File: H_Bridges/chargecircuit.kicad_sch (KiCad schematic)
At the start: 31 parts, among them J2 USB4085-GF-A_REVB, Q10 PMOS, Q9 PMOS, U2 max1898eub42+T, U3 TPS61023DRLR

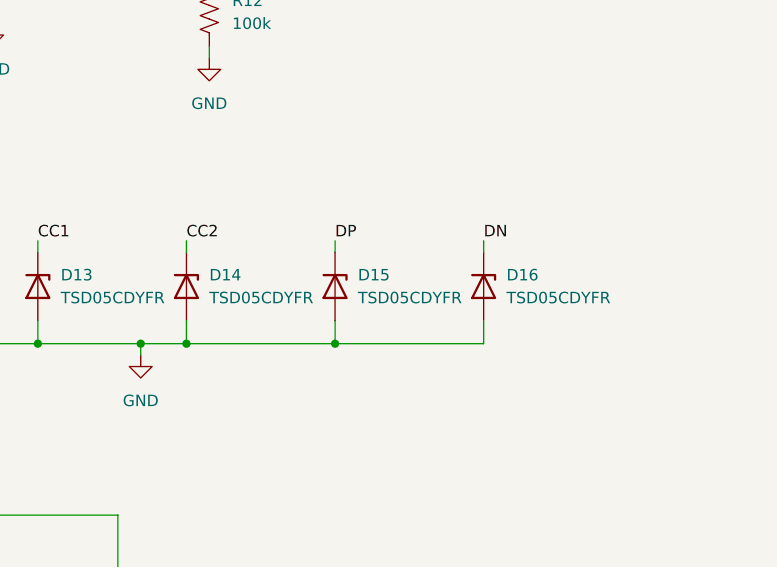
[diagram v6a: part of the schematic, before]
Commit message: placement fixes
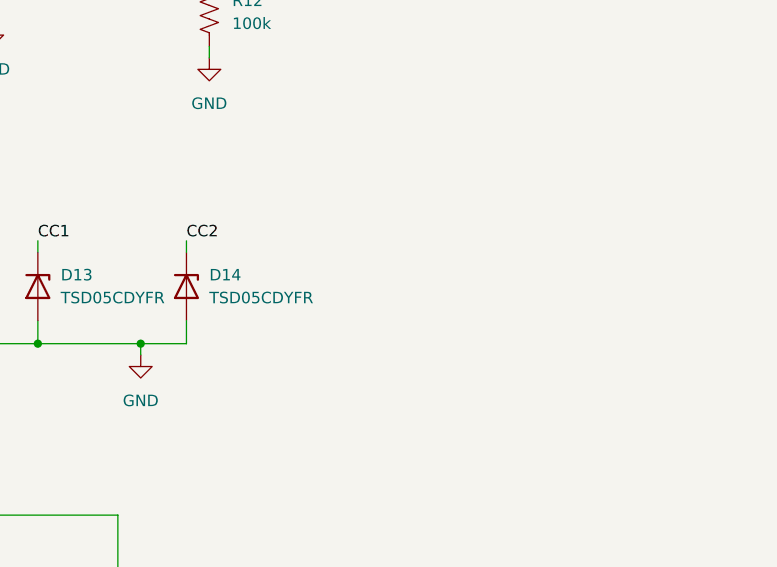
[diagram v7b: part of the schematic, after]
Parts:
- removed D15, D16: TSD05CDYFR, Footprints:TVS_SOD2_DYF_TEX-L, symbol Diode:PTVS5V0Z1USK
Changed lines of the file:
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@@
 	)
 	(junction
-		(at 241.3 91.44)
-		(diameter 0)
-		(color 0 0 0 0)
-	)
-	(junction
 		(at 173.99 138.43)
 		(diameter 0)
@@
 	)
 	(junction
-		(at 224.79 91.44)
-		(diameter 0)
-		(color 0 0 0 0)
-	)
-	(junction
 		(at 106.68 80.01)
 		(diameter 0)
@@
 	(wire
 		(pts
-			(xy 257.81 80.01) (xy 257.81 81.28)
-		)
-		(stroke
-			(width 0)
-			(type default)
-		)
-	)
-	(wire
-		(pts
 			(xy 147.32 110.49) (xy 152.4 110.49)
 		)
@@
 	(wire
 		(pts
-			(xy 241.3 88.9) (xy 241.3 91.44)
-		)
-		(stroke
-			(width 0)
-			(type default)
-		)
-	)
-	(wire
-		(pts
 			(xy 71.12 31.75) (xy 105.41 31.75)
 		)
@@
 	(wire
 		(pts
-			(xy 257.81 91.44) (xy 257.81 88.9)
-		)
-		(stroke
-			(width 0)
-			(type default)
-		)
-	)
-	(wire
-		(pts
 			(xy 189.23 88.9) (xy 189.23 91.44)
 		)
@@
 	(wire
 		(pts
-			(xy 224.79 91.44) (xy 241.3 91.44)
-		)
-		(stroke
-			(width 0)
-			(type default)
-		)
-	)
-	(wire
-		(pts
 			(xy 85.09 91.44) (xy 85.09 95.25)
 		)
@@
 	(wire
 		(pts
-			(xy 241.3 80.01) (xy 241.3 81.28)
-		)
-		(stroke
-			(width 0)
-			(type default)
-		)
-	)
-	(wire
-		(pts
 			(xy 80.01 97.79) (xy 82.55 97.79)
 		)
@@
 	(wire
 		(pts
-			(xy 241.3 91.44) (xy 257.81 91.44)
-		)
-		(stroke
-			(width 0)
-			(type default)
-		)
-	)
-	(wire
-		(pts
 			(xy 184.15 55.88) (xy 184.15 38.1)
 		)
@@
 		)
 	)
-	(label "DN"
-		(at 257.81 80.01 0)
-		(fields_autoplaced yes)
-		(effects
-			(font
-				(size 1.27 1.27)
-			)
-			(justify left bottom)
-		)
-	)
 	(label "DP"
 		(at 82.55 97.79 0)
@@
 		)
 	)
-	(label "DP"
-		(at 241.3 80.01 0)
-		(fields_autoplaced yes)
-		(effects
-			(font
-				(size 1.27 1.27)
-			)
-			(justify left bottom)
-		)
-	)
 	(label "CC1"
 		(at 208.28 80.01 0)
@@
 	)
 	(symbol
-		(lib_id "Diode:PTVS5V0Z1USK")
-		(at 257.81 85.09 270)
-		(unit 1)
-		(exclude_from_sim no)
-		(in_bom yes)
-		(on_board yes)
-		(dnp no)
-		(fields_autoplaced yes)
-		(property "Reference" "D16"
-			(at 260.35 83.8199 90)
-			(effects
-				(font
-					(size 1.27 1.27)
-				)
-				(justify left)
-			)
-		)
-		(property "Value" "TSD05CDYFR"
-			(at 260.35 86.3599 90)
-			(effects
-				(font
-					(size 1.27 1.27)
-				)
-				(justify left)
-			)
-		)
-		(property "Footprint" "Footprints:TVS_SOD2_DYF_TEX-L"
-			(at 253.365 85.09 0)
-			(effects
-				(font
-					(size 1.27 1.27)
-				)
-				(hide yes)
-			)
-		)
-		(property "Datasheet" ""
-			(at 257.81 85.09 0)
-			(effects
-				(font
-					(size 1.27 1.27)
-				)
-				(hide yes)
-			)
-		)
-		(property "Description" ""
-			(at 257.81 85.09 0)
-			(effects
-				(font
-					(size 1.27 1.27)
-				)
-				(hide yes)
-			)
-		)
-		(pin "1"
-		)
-		(pin "2"
-		)
-		(instances
-			(project "H_Bridges"
-				(path "/a020a591-cea5-4f16-9764-82374c05e734/4dadbc5e-54c4-496a-92da-5b0d288672d2"
-					(reference "D16")
-					(unit 1)
-				)
-			)
-		)
-	)
-	(symbol
 		(lib_id "USB4085-GF-A_REVB:USB4085-GF-A_REVB")
 		(at 69.85 102.87 0)
@@
 					(unit 1)
 				)
-			)
-		)
-	)
-	(symbol
-		(lib_id "Diode:PTVS5V0Z1USK")
-		(at 241.3 85.09 270)
-		(unit 1)
-		(exclude_from_sim no)
-		(in_bom yes)
-		(on_board yes)
-		(dnp no)
-		(fields_autoplaced yes)
-		(property "Reference" "D15"
-			(at 243.84 83.8199 90)
-			(effects
-				(font
-					(size 1.27 1.27)
-				)
-				(justify left)
-			)
-		)
-		(property "Value" "TSD05CDYFR"
-			(at 243.84 86.3599 90)
-			(effects
-				(font
-					(size 1.27 1.27)
-				)
-				(justify left)
-			)
-		)
-		(property "Footprint" "Footprints:TVS_SOD2_DYF_TEX-L"
-			(at 236.855 85.09 0)
-			(effects
-				(font
-					(size 1.27 1.27)
-				)
-				(hide yes)
-			)
-		)
-		(property "Datasheet" ""
-			(at 241.3 85.09 0)
-			(effects
-				(font
-					(size 1.27 1.27)
-				)
-				(hide yes)
-			)
-		)
-		(property "Description" ""
-			(at 241.3 85.09 0)
-			(effects
-				(font
-					(size 1.27 1.27)
-				)
-				(hide yes)
-			)
-		)
-		(pin "1"
-		)
-		(pin "2"
-		)
-		(instances
-			(project "H_Bridges"
-				(path "/a020a591-cea5-4f16-9764-82374c05e734/4dadbc5e-54c4-496a-92da-5b0d288672d2"
-					(reference "D15")
-					(unit 1)
-				)

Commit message: routing start
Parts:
- added H1, H2, H3, H4: MountingHole, MountingHole:MountingHole_3mm_Pad_TopBottom, symbol Mechanical:MountingHole
